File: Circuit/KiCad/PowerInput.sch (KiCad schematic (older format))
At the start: 23 parts

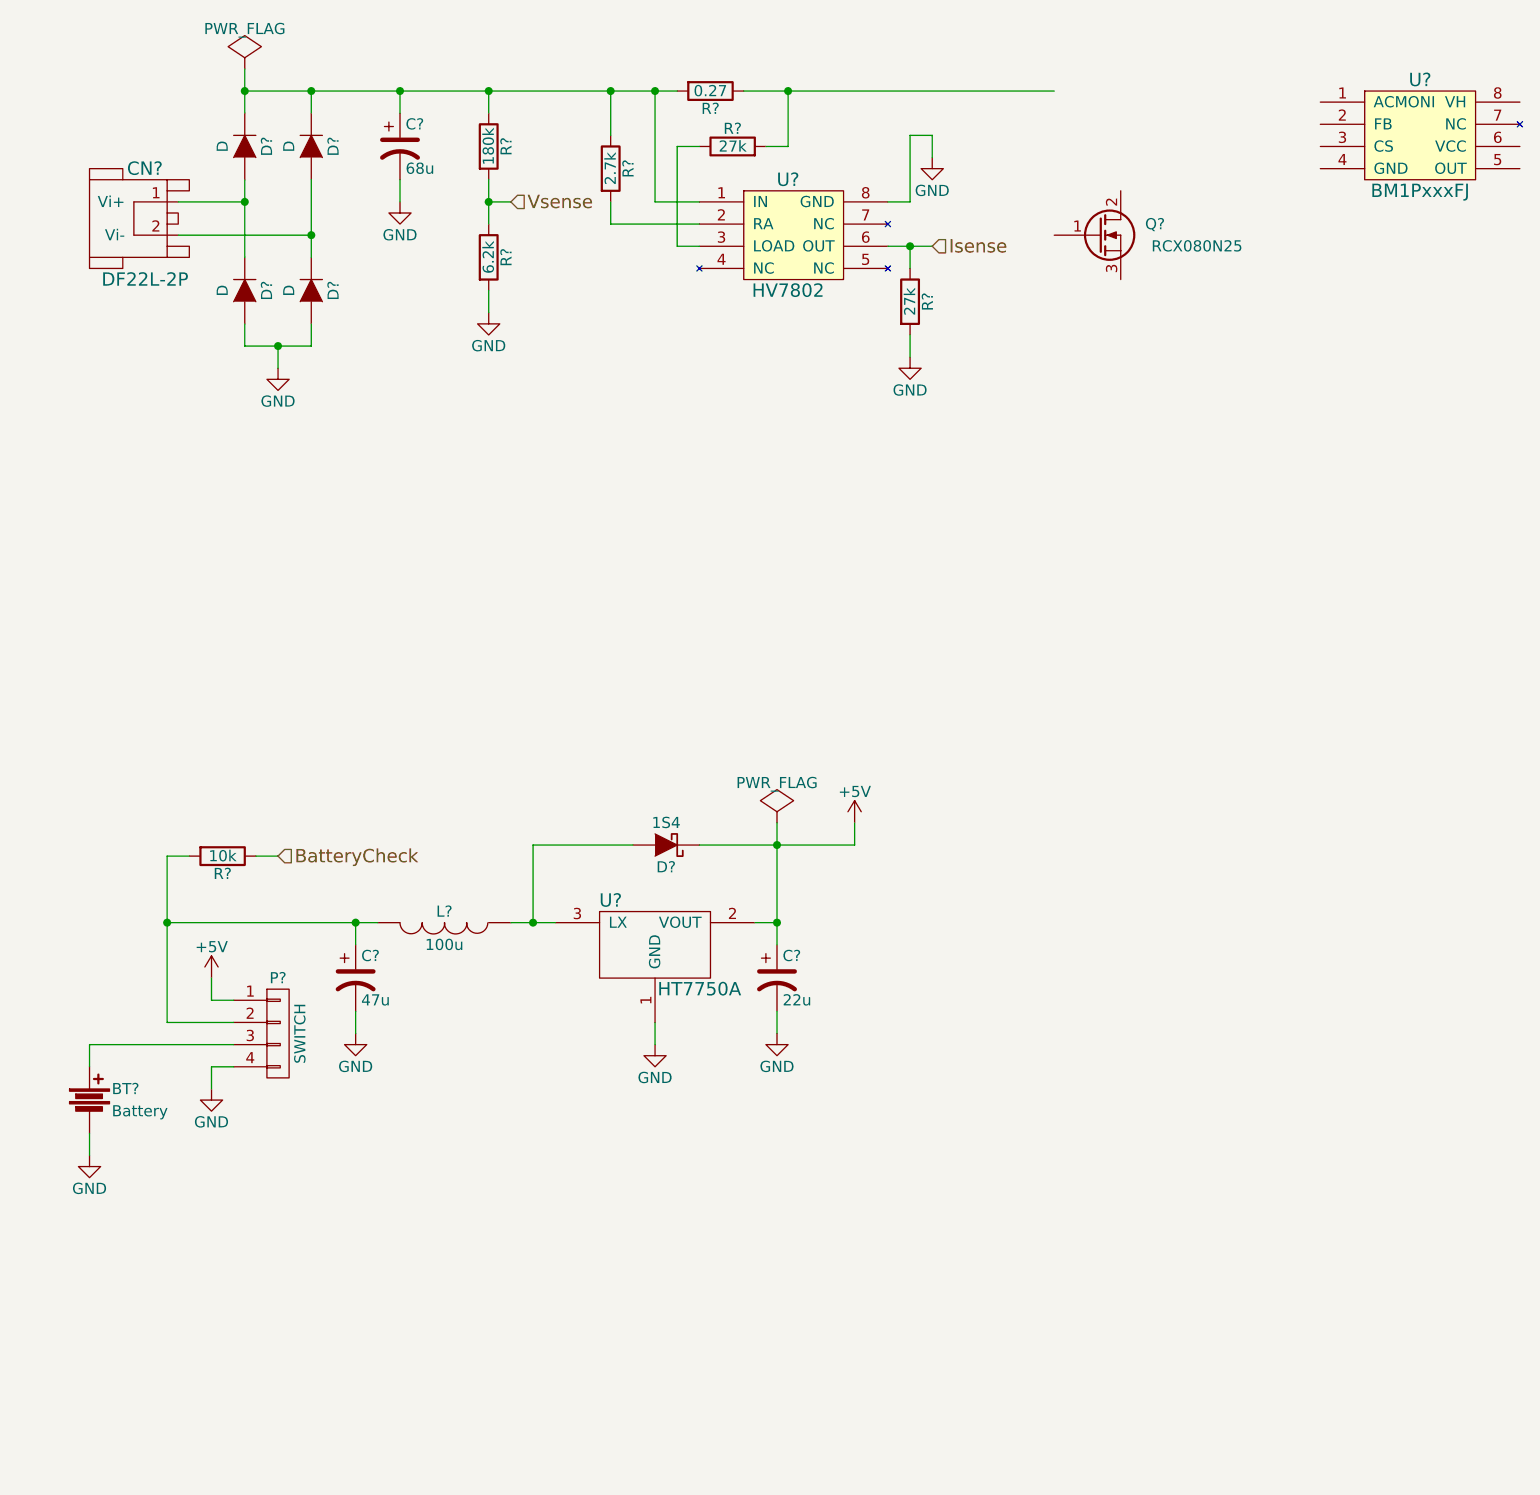
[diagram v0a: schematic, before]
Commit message: add LED driver
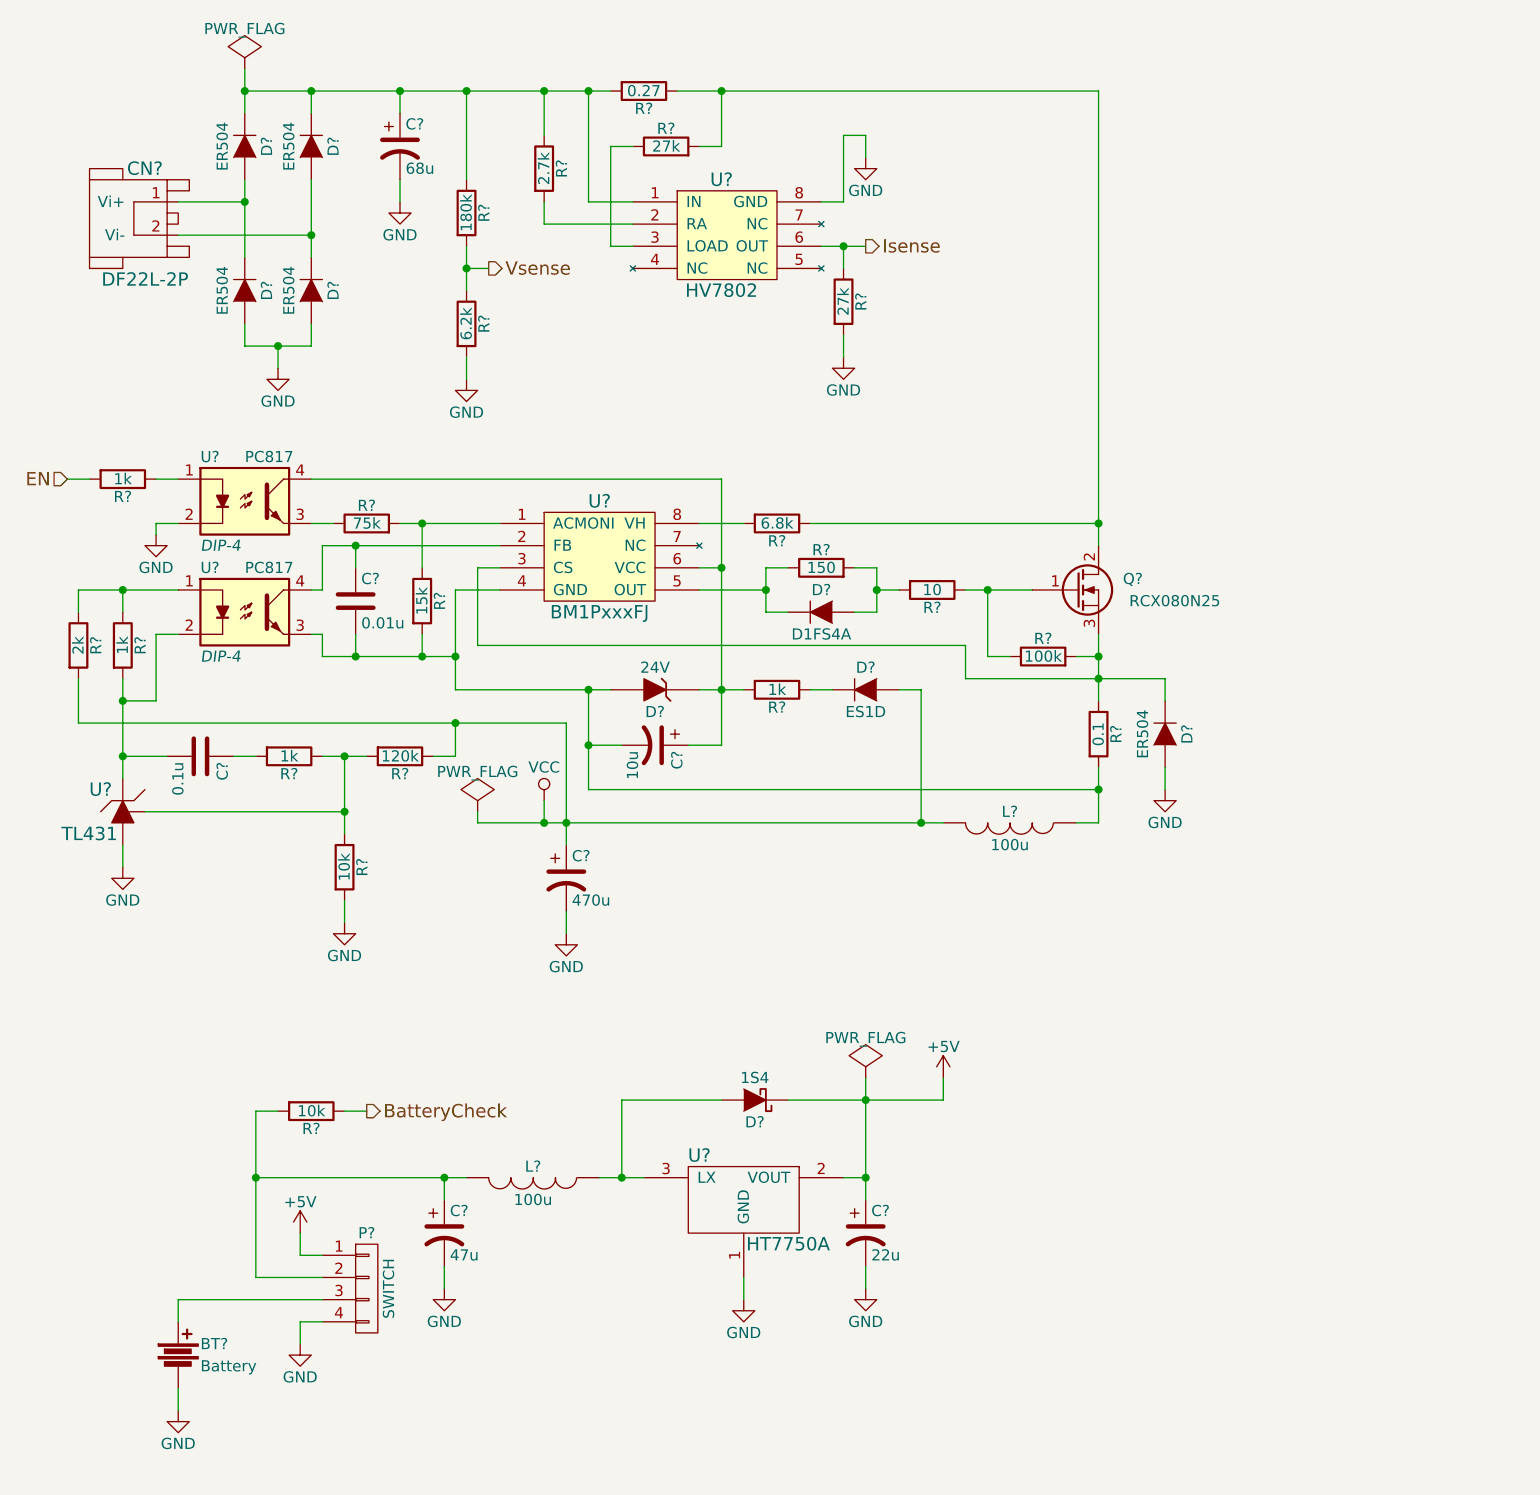
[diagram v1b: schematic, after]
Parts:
- added C?: 0.01u, symbol C
- added C?: 10u, symbol CP1
- added C?: 470u, symbol CP1
- added C?: 0.1u, symbol C
- added D?: ER504, symbol D
- added D?: 24V, symbol ZENER
- added D?: ES1D, symbol D
- added D?: D1FS4A, symbol D
- added L?: 100u, symbol INDUCTOR
- added R?: 75k, symbol R
- added R? (x4): 1k, symbol R
- added R?: 100k, symbol R
- added R?: 150, symbol R
- added R?: 10, symbol R
- added R?: 10k, symbol R
- added R?: 2k, symbol R
- added R?: 120k, symbol R
- added R?: 6.8k, symbol R
- added R?: 0.1, symbol R
- added R?: 15k, symbol R
- added U? (x2): PC817, DIP-4, symbol PC817
- added U?: TL431, symbol TL431
- D? (x4): value D -> ER504
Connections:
- net GND: now also C?.2, D?.2 (A), R?.2, U?.2, U?.2 (ANODE)
- net at R?.1, R?.2: now also Q?.2 (D), R?.1
- net at Q?.1 (G): now also R?.1, R?.1
- net at Q?.3 (S): now also U?.3 (CS), D?.1 (K), R?.1, R?.2
- net at U?.1 (ACMONI): now also R?.1, R?.2
- net at U?.2 (FB): now also C?.1, U?.4
- net at U?.4 (GND): now also C?.2, C?.2, D?.2 (A), L?.1, R?.2, R?.2, U?.3
- net at U?.5 (OUT): now also D?.1 (K), R?.1
- net at U?.6 (VCC): now also C?.1, D?.1 (K), R?.2, U?.4
- net at U?.8 (VH): now also R?.2
- new net: R?.1, R?.1, U?.1
- new net: C?.2, R?.2, U?.2, U?.3 (CATHODE)
- new net: R?.1, U?.3
- new net: D?.1 (K), R?.1
- new net: D?.2 (A), R?.2, R?.2
- new net: R?.1, R?.1, R?.2, U?.1 (REF)
- new net: R?.1, U?.1
- new net: C?.1, R?.2
- new net EN: R?.2
- new net VCC: C?.1, D?.2 (A), L?.2, R?.1, R?.2
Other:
- moved on the sheet: BT?, C?, D?, L?, P?, Q?, R?, U?

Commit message: EeSchema settled
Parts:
- added D34: 1S4, Diodes_ThroughHole:Diode_DO-41_SOD81_Vertical_AnodeUp, symbol D_Schottky
- BT1: renamed from BT?; footprint (none) -> Connect:bornier2
- C10, C12, C13: renamed from C?; footprint (none) -> Capacitors_Elko_ThroughHole:Elko_vert_11.2x6.3mm_RM2.5_CopperClear
- C11: renamed from C?; footprint (none) -> Capacitors_ThroughHole:C_Radial_D12.5_L25_P5
- C7, C8: renamed from C?; footprint (none) -> Capacitors_ThroughHole:C_Disc_D3_P2.5
- C9: renamed from C?; value 68u -> 100u; footprint (none) -> Capacitors_ThroughHole:C_Radial_D16_L25_P7.5
- CN1: renamed from CN?; footprint (none) -> user_conn:CONN_RED_2P
- D1, D2, D3, D4, D9: renamed from D?; footprint (none) -> Diodes_ThroughHole:Diode_DO-201AD_Horizontal_RM15
- D5, D6: renamed from D?; footprint (none) -> Diodes_ThroughHole:Diode_DO-41_SOD81_Vertical_AnodeUp
- D7: renamed from D?; footprint (none) -> Diodes_SMD:SMB_Handsoldering
- D8: renamed from D?; footprint (none) -> Diodes_SMD:SMA_Handsoldering
- L1: renamed from L?; footprint (none) -> Choke_SMD:Choke_SMD_10.4x10.4_H4.8
- L2: renamed from L?; footprint (none) -> Choke_Toroid_ThroughHole:Choke_Toroid_8x16mm_Vertical
- P4: renamed from P?; footprint (none) -> Connect:bornier4
- Q1: renamed from Q?; footprint (none) -> Transistors_TO-220:TO-220_Neutral123_Horizontal_LargePads
- R1, R15, R16, R17, R19, R2, R20, R3, R4, R5, R6, R7, R8, R9: renamed from R?; footprint (none) -> Discret:R3-5
- R10, R11, R12, R14, R18: renamed from R?; footprint (none) -> Resistors_SMD:R_0603_HandSoldering
- R13: renamed from R?; footprint (none) -> Resistors_SMD:R_2512_HandSoldering
- R21: renamed from R?; footprint (none) -> Discret:R6
- U2, U7: renamed from U?; footprint (none) -> Housings_TO-92:TO-92_Inline_Wide
- U3, U4: renamed from U?; footprint DIP-4 -> Housings_DIP:DIP-4_W7.62mm
- U5: renamed from U?; value BM1PxxxFJ -> BM1P061FJ; footprint (none) -> Housings_SOIC:SOIC-8_3.9x4.9mm_Pitch1.27mm
- U6: renamed from U?; footprint (none) -> Housings_SSOP:MSOP-8_3x3mm_Pitch0.65mm
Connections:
- net at C10.1, L1.2, R5.2: now also D34.1 (K); no longer P4.2 (P2)
- new net: D34.2 (A), P4.2 (P2)
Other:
- moved on the sheet: BT1, P4, R5
